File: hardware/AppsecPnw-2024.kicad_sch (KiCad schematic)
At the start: 40 parts, among them J1 OLED, J2 Battery, J3 I2C, J4 UART, P1 USB_C_Plug_USB2.0, Q1 DMG3415U-7, Q2 MMBT2222A, SW1 ON, SW2 LEFT, SW3 DOWN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

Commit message: feat(Hw) Init PCB
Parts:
- BZ1: footprint Footprint:Buzzer4x4 -> Footprints:Buzzer4x4
- J2: footprint Footprint:BAT-TH_BH-AAA-A1AJ024 -> Footprints:BAT-TH_BH-AAA-A1AJ024
- P1: footprint Footprint:C393939 -> Footprints:C393939
- R2: footprint Resistor_SMD:R_0603_1608Metric_Pad0.98x0.95mm_HandSolder -> Resistor_SMD:R_0603_1608Metric
- SW1: footprint Footprint:JS102011SAQN -> Footprints:JS102011SAQN
- U1: footprint Footprint:MOD28_ESP32-C6-WROOM-1U_EXP -> Footprints:MOD28_ESP32-C6-WROOM-1U_EXP
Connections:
- net +3V3: now also J1.3 (Pin_3); no longer J1.1 (Pin_1)
- net GND: now also J1.4 (Pin_4); no longer J1.2 (Pin_2)
- net SCL: now also J1.2 (Pin_2); no longer J1.3 (Pin_3)
- net SDA: now also J1.1 (Pin_1); no longer J1.4 (Pin_4)
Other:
- moved on the sheet: C14, C15, D3, D4, J1, R4, R5, R8, SW6, SW7

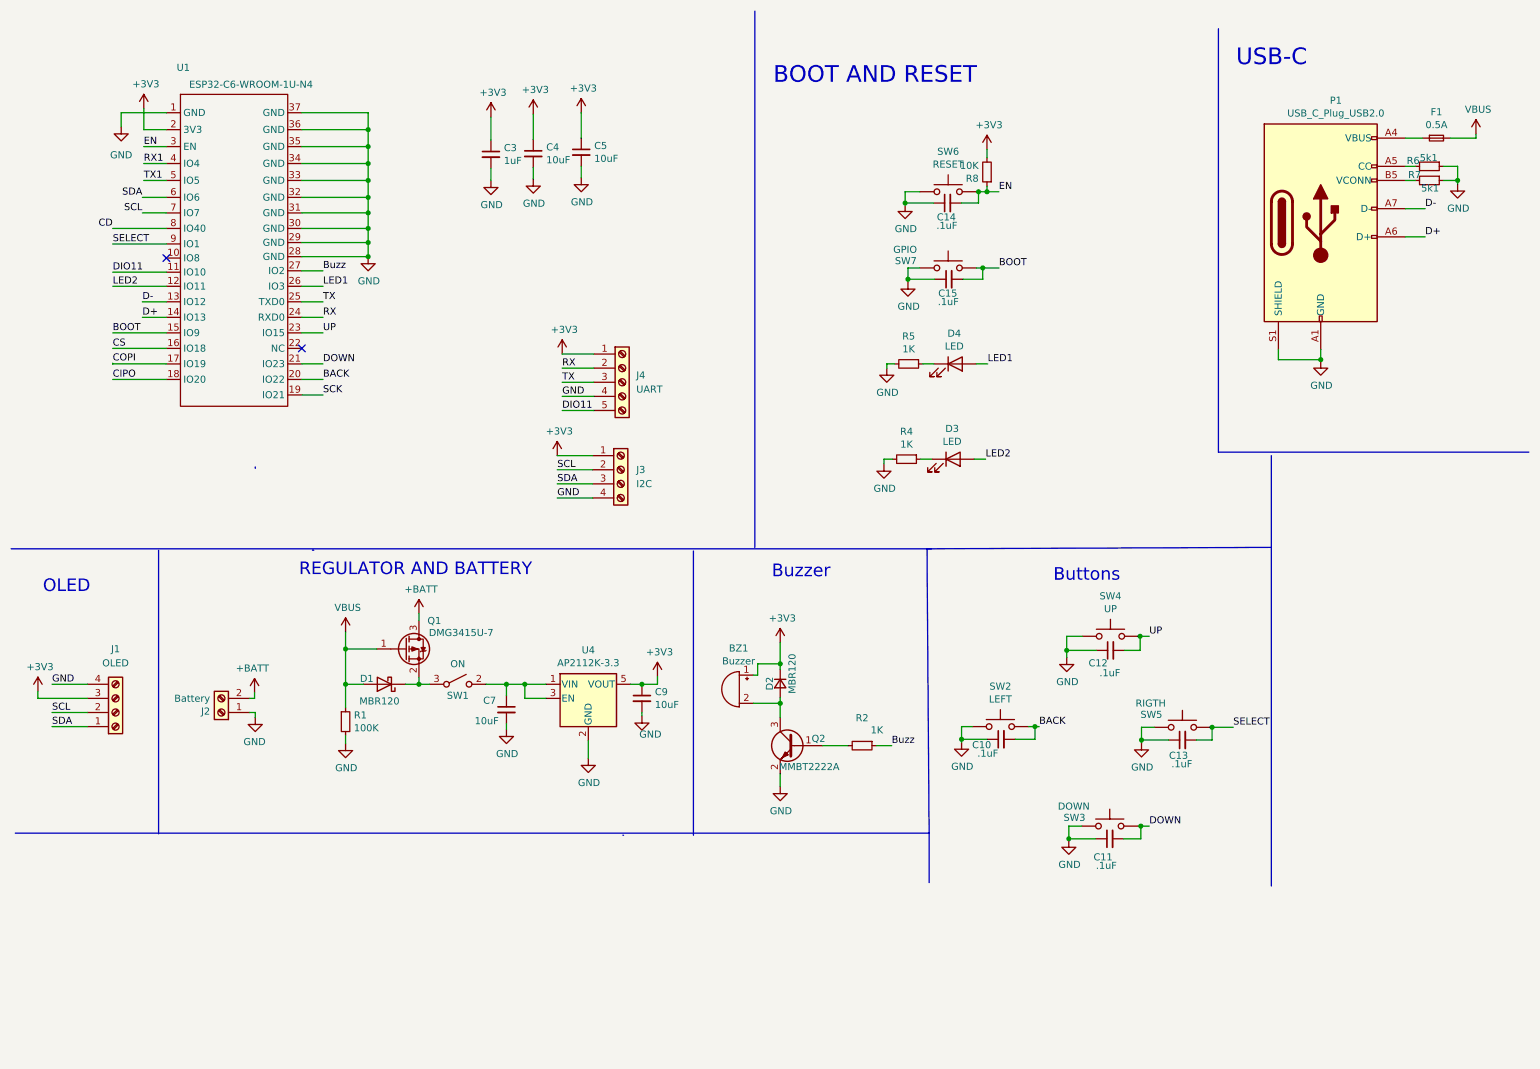
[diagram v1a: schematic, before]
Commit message: feat(Hw) Update schematic and floorplan
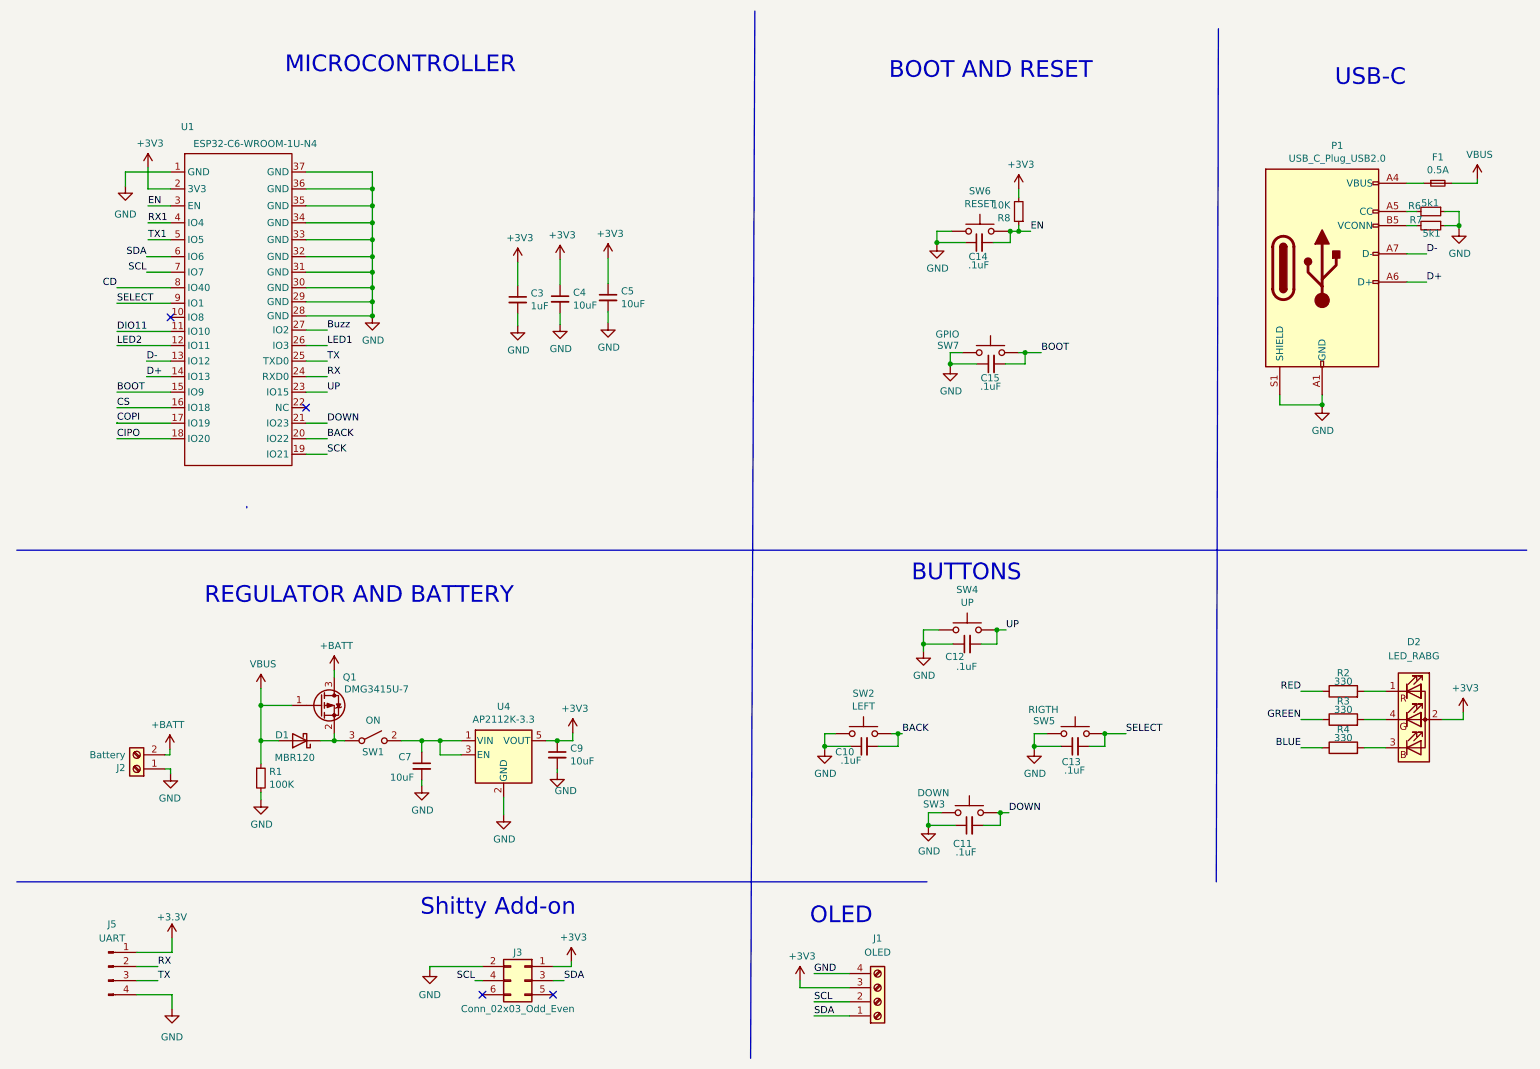
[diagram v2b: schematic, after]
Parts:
- removed BZ1: Buzzer, Footprints:Buzzer4x4, symbol Device:Buzzer
- removed D2: MBR120, Diode_SMD:D_SOD-123F, symbol Device:D_Small
- removed D3, D4: LED, LED_SMD:LED_0805_2012Metric_Pad1.15x1.40mm_HandSolder, symbol Device:LED
- removed J3: I2C, Connector_PinHeader_2.54mm:PinHeader_1x04_P2.54mm_Vertical, symbol Connector:Screw_Terminal_01x04
- removed J4: UART, Connector_PinHeader_2.54mm:PinHeader_1x05_P2.54mm_Vertical, symbol Connector:Screw_Terminal_01x05
- removed Q2: MMBT2222A, Package_TO_SOT_SMD:SOT-23, symbol Transistor_BJT:PN2222A
- removed R2, R4, R5: 1K, Resistor_SMD:R_0603_1608Metric, symbol Device:R_Small
- added D2: LED_RABG, Footprints:AAA3528SURKCGKC09, symbol Device:LED_RABG
- added J3: Conn_02x03_Odd_Even, Connector_PinSocket_2.54mm:PinSocket_2x03_P2.54mm_Vertical, symbol Connector_Generic:Conn_02x03_Odd_Even
- added J5: UART, Footprints:PinHeader_1x04_P2.54mm_Vertical, symbol Connector:Conn_01x04_Pin
- added R2, R3, R4: 330, Resistor_SMD:R_0603_1608Metric, symbol Device:R
- C10, C11, C12, C13, C14, C15, C3, C4, C5, C7, C9, D1, SW2, SW3, SW4, SW5, SW6, SW7, U4: provedor LCSC -> (none)
- F1, SW1: provedor MOUSER -> (none)
- J1: footprint Connector_PinHeader_2.54mm:PinHeader_1x04_P2.54mm_Vertical -> Footprints:Display OLED 128 x32; Proveedor (none) -> UNIT; manf# I2C SH1106 Display Oled Azul 128×64 1.3 ” -> Display OLED 128×32 0.91 I2C SSD1306 Blanco / Azul; provedor UNIT Electronics -> (none)
- J2: provedor - -> (none)
- P1: LCSC# C2987386 -> C2760486; manf# TYPE-C-31-M-31 -> (none); provedor LCSC -> (none)
- Q1: manf# DMG3415U-7 -> (none); provedor LCSC -> (none)
- R1: Proveedor LCSC -> (none); provedor LCSC -> (none)
- R6, R7: manf# ERJ3RBD5101V -> (none); provedor LCSC -> (none)
- R8: manf# CR-03JL7---10K -> (none); provedor LCSC -> (none)
- U1: manf# ESP32-C6-WROOM-1U-N4 -> ESP32-C6-WROOM-1-N4; provedor MOUSER -> (none)
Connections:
- net +3V3: now also D2.2 (A), J3.1 (Pin_1)
- net GND: now also J3.2 (Pin_2), J5.4 (Pin_4)
- net RX: now also J5.2 (Pin_2)
- net SCL: now also J3.4 (Pin_4)
- net SDA: now also J3.3 (Pin_3)
- net TX: now also J5.3 (Pin_3)
- new net: D2.3 (BK), R4.2
- new net: D2.1 (RK), R2.2
- new net: D2.4 (GK), R3.2
- new net +3.3V: J5.1 (Pin_1)
- new net BLUE: R4.1
- new net GREEN: R3.1
- new net RED: R2.1
- no-connect marks 2 -> 4
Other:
- note added: "BUTTONS"
- note added: "MICROCONTROLLER"
- note added: "Shitty Add-on"
- note removed: "Buttons"
- note removed: "Buzzer"
- company: (none) -> Electronic Cats
- title: (none) -> ApsecPnw-2024
- moved on the sheet: C10, C11, C12, C13, C14, C15, C3, C4, C5, C7, C9, D1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

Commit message: feat(Hw) Update schematic
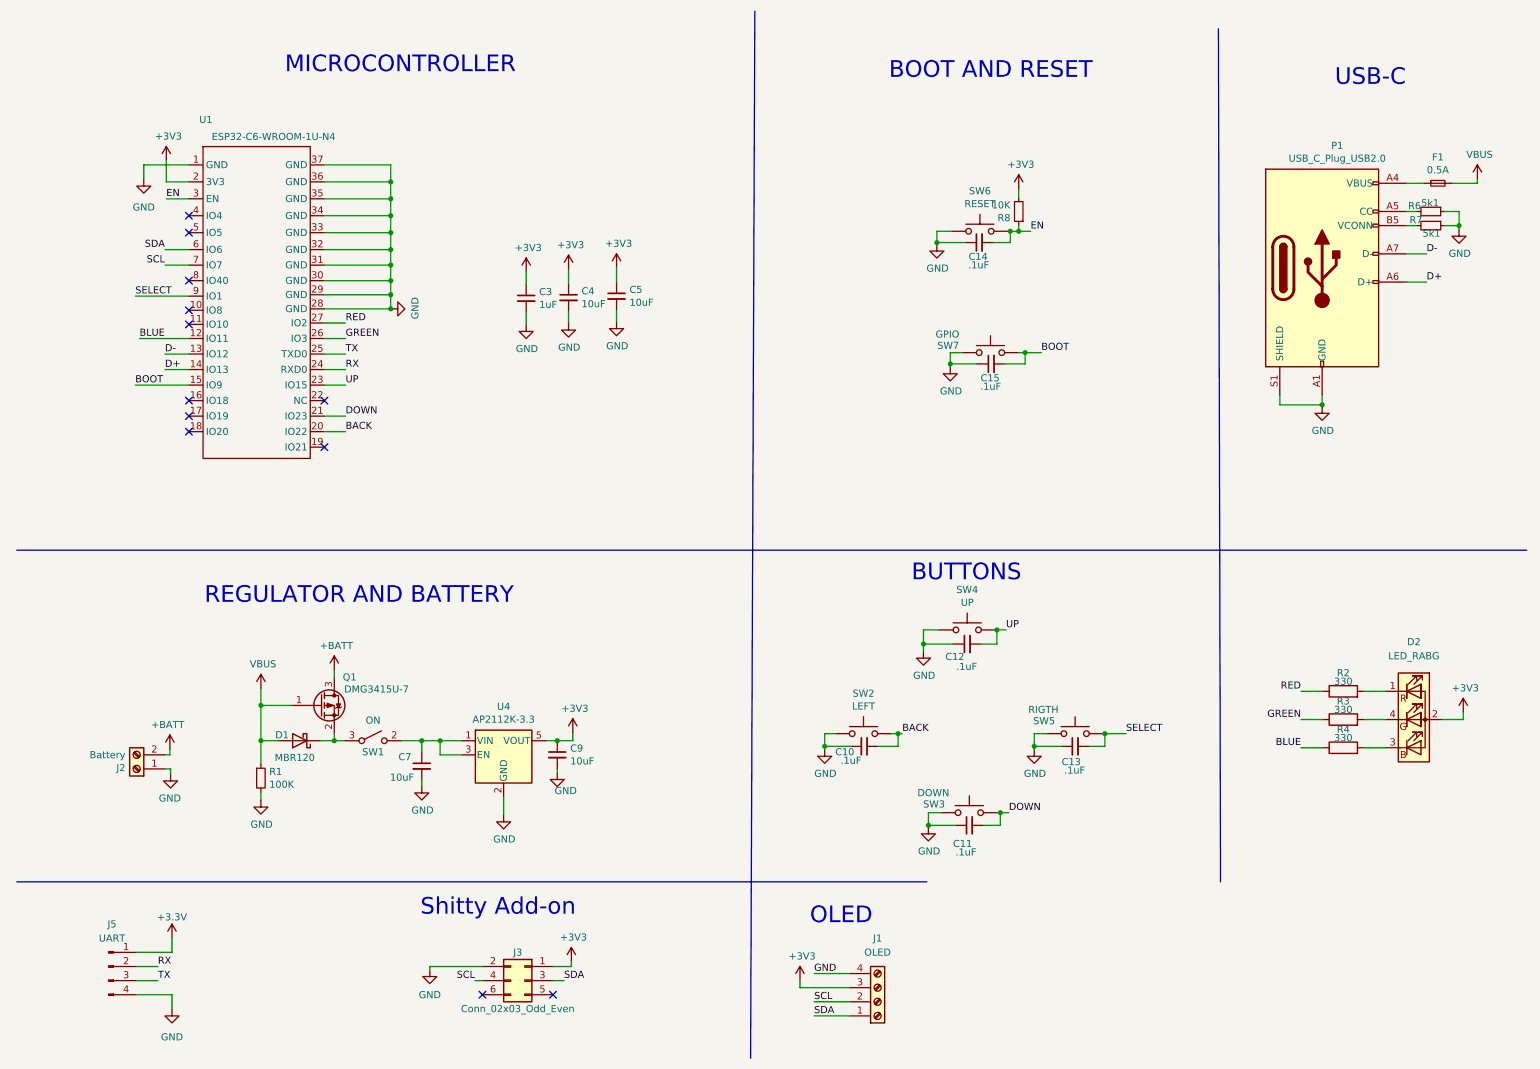
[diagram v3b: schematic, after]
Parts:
- J1: manf# Display OLED 128×32 0.91 I2C SSD1306 Blanco / Azul -> Display Oled Azul y Blanco 128×64 0.96″ I2C SSD1306
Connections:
- net Buzz is gone; now on net RED: U1.27 (IO2)
- net LED1 is gone; now on net GREEN: U1.26 (IO3)
- net LED2 is gone; now on net BLUE: U1.12 (IO11)
- net CD: no longer names the net of U1.8 (IO40)
- net CIPO: no longer names the net of U1.18 (IO20)
- net COPI: no longer names the net of U1.17 (IO19)
- net CS: no longer names the net of U1.16 (IO18)
- net DIO11: no longer names the net of U1.11 (IO10)
- net RX1: no longer names the net of U1.4 (IO4)
- net SCK: no longer names the net of U1.19 (IO21)
- net TX1: no longer names the net of U1.5 (IO5)
- no-connect marks 4 -> 12
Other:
- moved on the sheet: C3, C4, C5, U1

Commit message: feat(Hw): Update schematic and init route
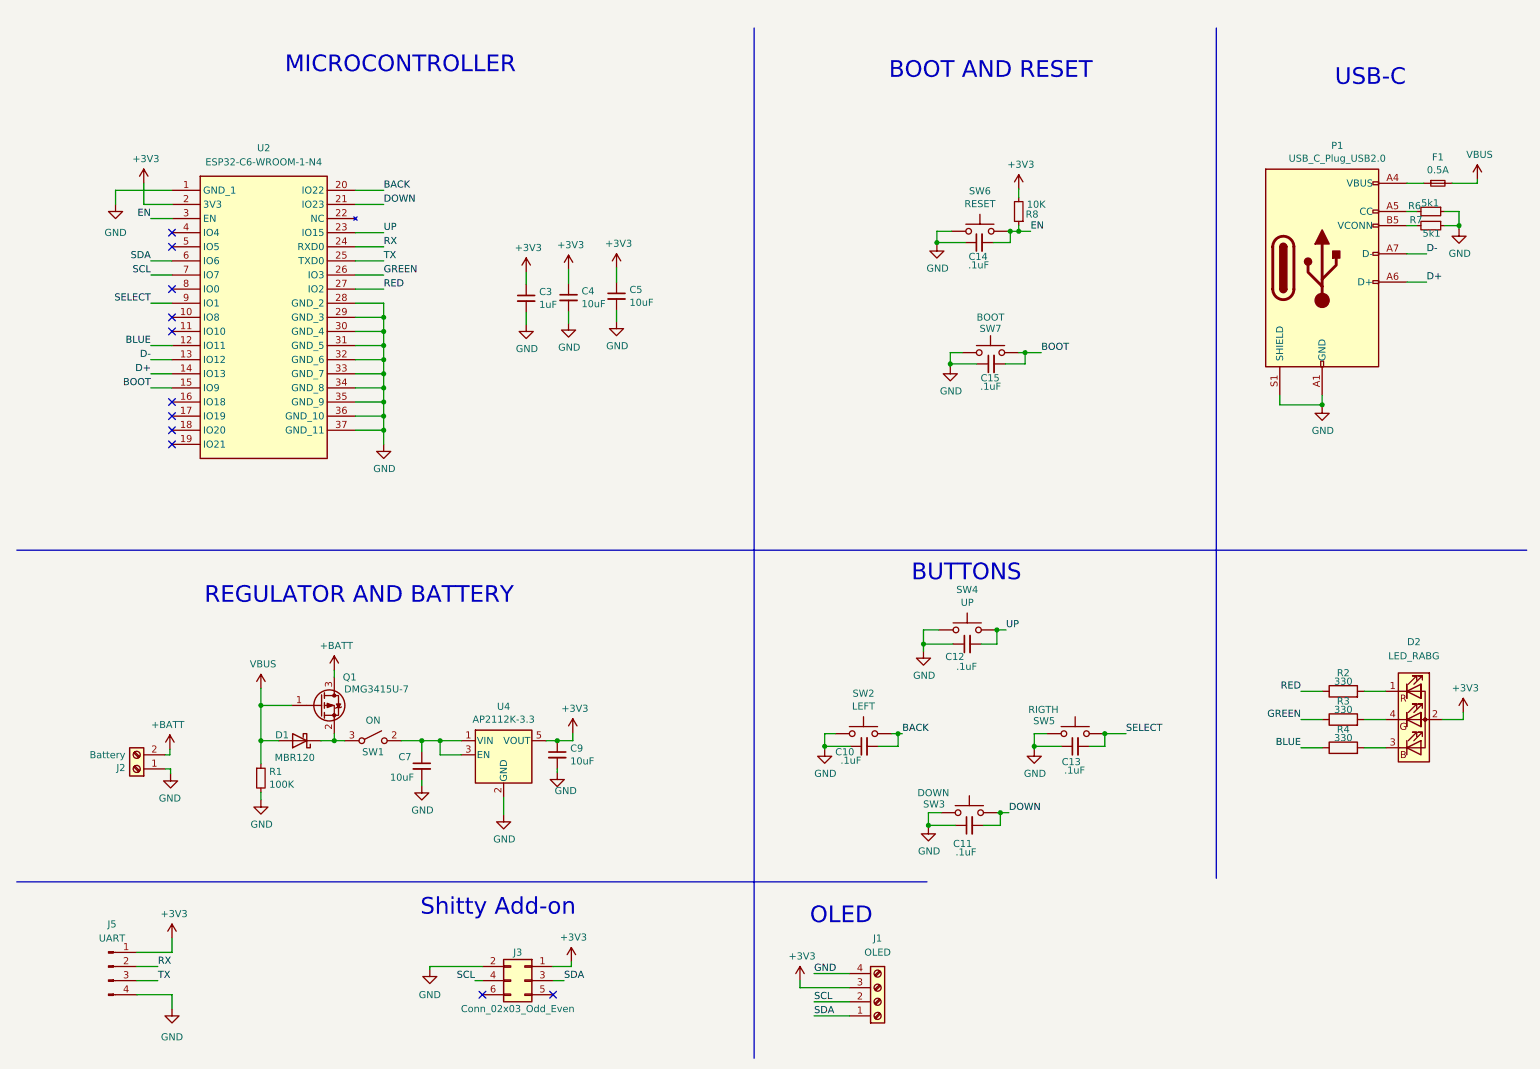
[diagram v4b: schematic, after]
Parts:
- removed U1: ESP32-C6-WROOM-1U-N4, Footprints:MOD28_ESP32-C6-WROOM-1U_EXP, symbol Minino:ESP32-C6-WROOM-1U-N8
- added U2: ESP32-C6-WROOM-1-N4, Footprints:ESP32C6WROOM1N4, symbol ESP32-C6-WROOM-1-N4:ESP32-C6-WROOM-1-N4
- SW7: value GPIO -> BOOT
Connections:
- net +3.3V is gone; now on net +3V3: J5.1 (Pin_1)
- net +3V3: now also U2.2 (3V3)
- net BACK: now also U2.20 (IO22)
- net BLUE: now also U2.12 (IO11)
- net BOOT: now also U2.15 (IO9)
- net D+: now also U2.14 (IO13)
- net D-: now also U2.13 (IO12)
- net DOWN: now also U2.21 (IO23)
- net EN: now also U2.3 (EN)
- net GND: now also U2.1 (GND_1), U2.28 (GND_2), U2.29 (GND_3), U2.30 (GND_4), U2.31 (GND_5), U2.32 (GND_6), U2.33 (GND_7), U2.34 (GND_8), U2.35 (GND_9), U2.36 (GND_10), U2.37 (GND_11)
- net GREEN: now also U2.26 (IO3)
- net RED: now also U2.27 (IO2)
- net RX: now also U2.24 (RXD0)
- net SCL: now also U2.7 (IO7)
- net SDA: now also U2.6 (IO6)
- net SELECT: now also U2.9 (IO1)
- net TX: now also U2.25 (TXD0)
- net UP: now also U2.23 (IO15)
- no-connect marks 12 -> 11

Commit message: feat(Hw): Update BOM
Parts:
- R6, R7: LCSC# C191782 -> C311919
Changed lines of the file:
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@@
 	(title_block
 		(title "ApsecPnw-2024")
-		(date "2024-04-01")
-		(rev "v1.0")
+		(date "2024-04-10")
+		(rev "v2.0")
 		(company "Electronic Cats")
 	)
@@
 			)
 		)
-		(property "LCSC#" "C191782"
+		(property "LCSC#" "C311919"
 			(at 267.208 45.72 0)
 			(effects
@@
 			)
 		)
-		(property "LCSC#" "C191782"
+		(property "LCSC#" "C311919"
 			(at 267.208 48.26 0)
 			(effects

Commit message: fix(Hw): Change F1
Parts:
- F1: value 0.5A -> 1A; LCSC# - -> C2649564; manf# MFU0805FF00500P100 -> MFU0805FF01000P100
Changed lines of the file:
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@@
 			)
 		)
-		(property "Value" "0.5A"
+		(property "Value" "1A"
 			(at 268.478 38.2524 0)
 			(effects
@@
 			)
 		)
-		(property "manf#" "MFU0805FF00500P100"
+		(property "manf#" "MFU0805FF01000P100"
 			(at 268.478 40.64 0)
 			(effects
@@
 			)
 		)
-		(property "LCSC#" "-"
+		(property "LCSC#" "C2649564"
 			(at 268.478 40.64 0)
 			(effects
